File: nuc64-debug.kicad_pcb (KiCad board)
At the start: 2 copper layers, 17.1 x 22.9 mm, 10 parts, among them J1 SWD, J2 POW, SW1 BOOT, SW2 RST

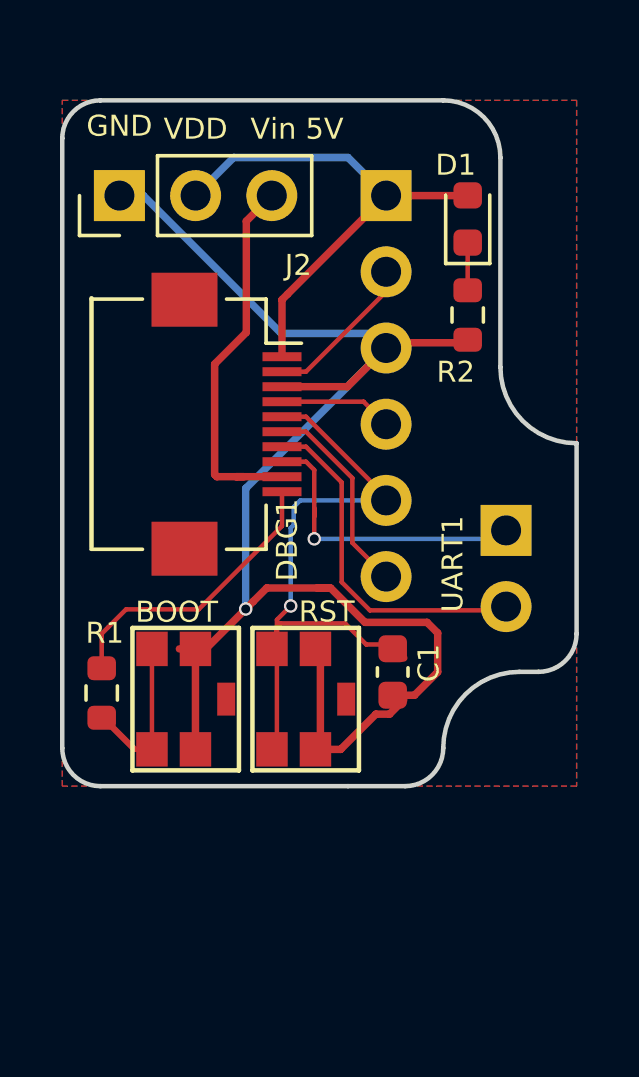
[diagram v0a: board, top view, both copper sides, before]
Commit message: [#32/#388] Boot0-button pulls high; updated symbols
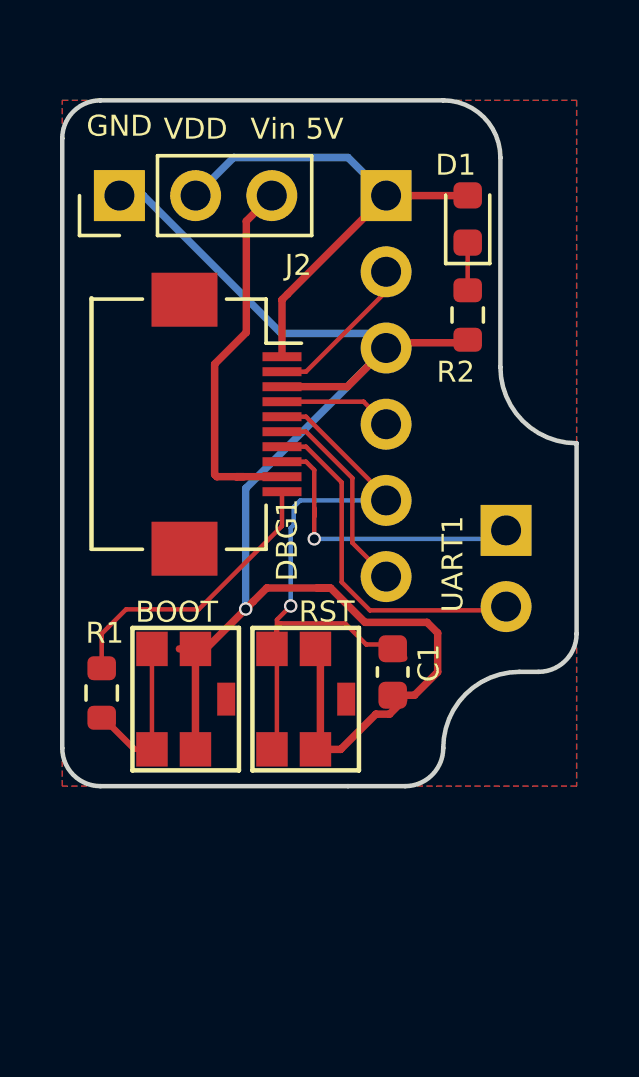
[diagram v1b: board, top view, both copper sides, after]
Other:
- net class Default removed
- net class power removed
- board text added: "CAMPO.SEESSLEN.NET NUC64DEBUG V0.3.x"
- board text removed: "CAMPO.SEESSLEN.NET NUC64DEBUG V0.2.x 20210714"

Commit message: Finished routing
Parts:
- added C2: 100n, Capacitor_SMD:C_0603_1608Metric, B.Cu at (112.0, 94.0)
- added R3: 330, Resistor_SMD:R_0603_1608Metric, B.Cu at (120.0, 94.0)
- C1, R1: moved to B.Cu
- D1: value LED -> LED Violet
- DBG1: footprint footprints:Hirose_FH12-10S-0.5SH_1x10_P0.5mm_Horizontal -> Connector_FFC-FPC:Hirose_FH12-10S-0.5SH_1x10-1MP_P0.50mm_Horizontal
- R2: value R -> 2K
- SW1, SW2: footprint footprints:panasonic_evpa302k -> Button_Switch_SMD:SW_SPST_Omron_B3FS-105xP
- moved SW2 6.48 mm to (120.7, 92.7)
- moved C1 5.02 mm to (120.0, 92.0), turned to 180 degrees
- moved SW1 4.80 mm to (112.3, 92.7)
- moved R1 4.79 mm to (112.0, 92.0), turned to 180 degrees
- moved J2 2.54 mm to (110.5, 68.6)
- moved DBG1 1.74 mm to (113.5, 78.8)
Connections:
- D1 pad 2: /VDD -> VDD
- DBG1 pad 1: /VDD -> VDD
- J1 pad 1: /VDD -> VDD
- J2 pad 2: /VDD -> VDD
- SW1 pad 2: GND -> VDD
- SW2 pad 1: /NRST -> Net-(R3-Pad2)
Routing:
- net VDD: track 0.00 -> 50.4 mm, vias 0 -> 1
- net GND: track 52.0 -> 99.0 mm, vias 1 -> 8
- net /VDD: track 17.0 -> 0.00 mm
- net Net-(R3-Pad2): track 0.00 -> 14.3 mm, vias 0 -> 1
- net Net-(R1-Pad2): track 7.05 -> 15.8 mm, vias 0 -> 1
- net Net-(DBG1-Pin_8): track 10.3 -> 17.3 mm, vias 1 -> 0
- net Net-(DBG1-Pin_10): track 9.79 -> 14.9 mm, vias 0 -> 1
- net /NRST: track 22.7 -> 18.5 mm, vias 1 -> 0
- net Net-(DBG1-Pin_7): track 11.7 -> 12.8 mm
- net Net-(DBG1-Pin_9): track 12.6 -> 13.3 mm
- net /SWDIO: track 3.78 -> 4.34 mm
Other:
- board size 17.1 x 22.9 mm -> 17.1 x 31.8 mm
- board text added: "20260117"

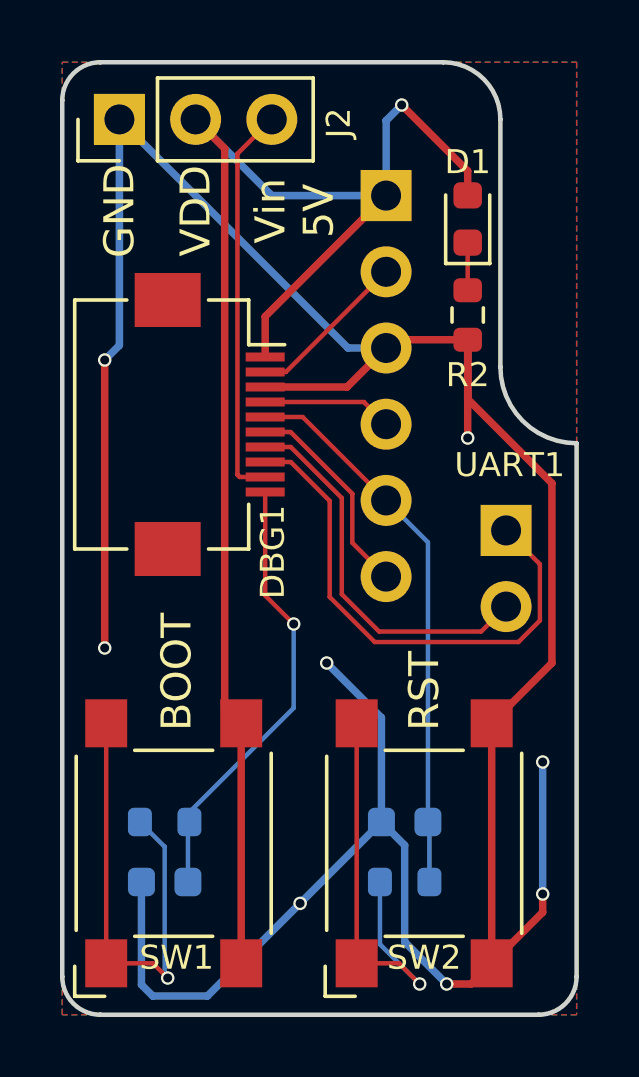
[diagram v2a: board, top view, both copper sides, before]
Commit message: Fixed trace width
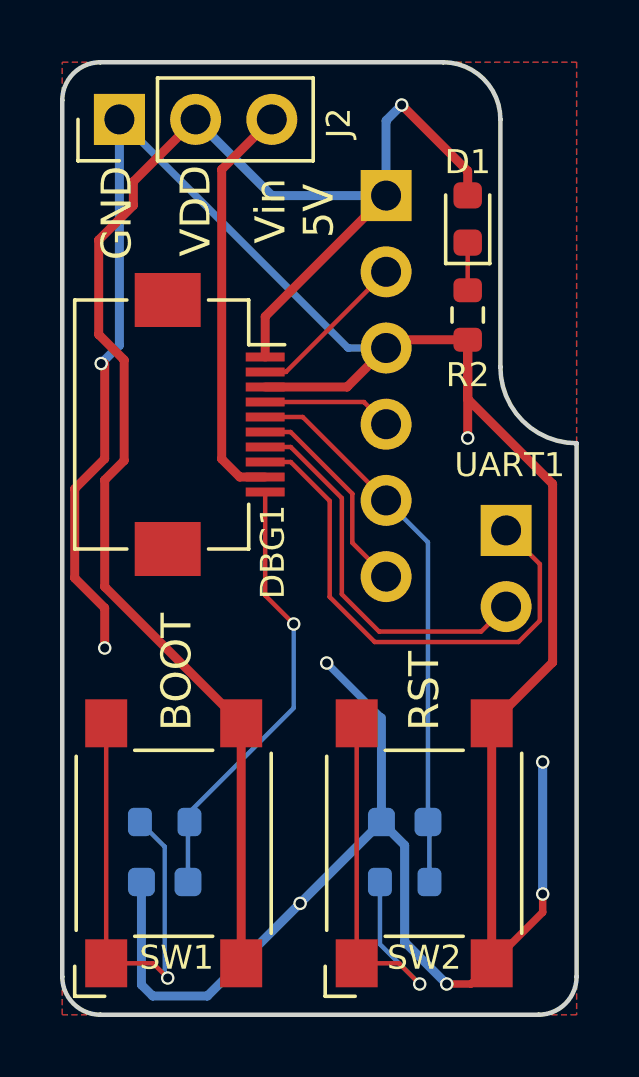
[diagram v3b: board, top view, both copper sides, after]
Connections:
- net Net-(DBG1-Pin_9) renamed VBUS
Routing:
- net VDD: track 50.4 -> 53.6 mm
- net GND: track 99.0 -> 100.0 mm
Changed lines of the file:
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@@
 	(net 8 "Net-(D1-K)")
 	(net 9 "VDD")
-	(net 10 "Net-(DBG1-Pin_9)")
+	(net 10 "VBUS")
 	(net 11 "Net-(DBG1-Pin_8)")
 	(net 12 "Net-(DBG1-Pin_7)")
@@
 			(layers "*.Cu" "*.Mask")
 			(remove_unused_layers no)
-			(net 10 "Net-(DBG1-Pin_9)")
+			(net 10 "VBUS")
 			(pinfunction "Pin_3")
 			(pintype "passive")
@@
 			(size 0.3 1.3)
 			(layers "F.Cu" "F.Mask" "F.Paste")
-			(net 10 "Net-(DBG1-Pin_9)")
+			(net 10 "VBUS")
 			(pinfunction "Pin_9")
 			(pintype "passive")
@@
 	)
 	(gr_text "GND"
-		(at 110.49 71.628 90)
+		(at 110.4 71.7 90)
 		(layer "F.SilkS")
 		(effects
@@
 		(start 122.1 75.925)
 		(end 119.655 75.925)
-		(width 0.25)
+		(width 0.3)
 		(layer "F.Cu")
 		(net 5)
 	)
 	(segment
-		(start 110 76.6)
-		(end 110 86.2)
-		(width 0.25)
+		(start 110 84.867106)
+		(end 109 83.867106)
+		(width 0.3)
 		(layer "F.Cu")
 		(net 5)
 	)
 	(segment
-		(start 122.1 77.9)
-		(end 122.1 75.925)
-		(width 0.25)
+		(start 109 83.867106)
+		(end 109 80.892893)
+		(width 0.3)
 		(layer "F.Cu")
 		(net 5)
@@
 		(start 122.1 75.925)
 		(end 122.1 79.2)
-		(width 0.25)
+		(width 0.3)
+		(layer "F.Cu")
+		(net 5)
+	)
+	(segment
+		(start 124.931 80.731)
+		(end 124.931 86.679)
+		(width 0.3)
+		(layer "F.Cu")
+		(net 5)
+	)
+	(segment
+		(start 124.931 86.679)
+		(end 122.9 88.71)
+		(width 0.3)
 		(layer "F.Cu")
 		(net 5)
@@
 		(start 115.35 77.5)
 		(end 118.08 77.5)
-		(width 0.25)
+		(width 0.3)
 		(layer "F.Cu")
 		(net 5)
 	)
 	(segment
-		(start 124.907 80.707)
-		(end 122.1 77.9)
-		(width 0.25)
+		(start 110 79.892894)
+		(end 110 76.734884)
+		(width 0.3)
 		(layer "F.Cu")
 		(net 5)
 	)
 	(segment
-		(start 124.907 86.703)
-		(end 124.907 80.707)
-		(width 0.25)
+		(start 109 80.892893)
+		(end 110 79.892894)
+		(width 0.3)
 		(layer "F.Cu")
 		(net 5)
 	)
 	(segment
-		(start 122.9 96.71)
-		(end 122.9 88.71)
-		(width 0.25)
+		(start 110 76.734884)
+		(end 109.982558 76.717442)
+		(width 0.3)
 		(layer "F.Cu")
 		(net 5)
 	)
 	(segment
-		(start 122.9 88.71)
-		(end 124.907 86.703)
-		(width 0.25)
+		(start 122.9 96.71)
+		(end 122.9 88.71)
+		(width 0.3)
 		(layer "F.Cu")
 		(net 5)
@@
 	)
 	(segment
+		(start 122.1 75.925)
+		(end 122.1 77.9)
+		(width 0.3)
+		(layer "F.Cu")
+		(net 5)
+	)
+	(segment
 		(start 118.08 77.5)
 		(end 119.38 76.2)
-		(width 0.25)
+		(width 0.3)
+		(layer "F.Cu")
+		(net 5)
+	)
+	(segment
+		(start 109.982558 76.717442)
+		(end 109.882558 76.717442)
+		(width 0.3)
 		(layer "F.Cu")
 		(net 5)
@@
 		(net 5)
 	)
+	(segment
+		(start 122.1 77.9)
+		(end 124.931 80.731)
+		(width 0.3)
+		(layer "F.Cu")
+		(net 5)
+	)
+	(segment
+		(start 110 86.2)
+		(end 110 84.867106)
+		(width 0.3)
+		(layer "F.Cu")
+		(net 5)
+	)
 	(via
 		(at 124.6 94.4)
@@
 	)
 	(via
-		(at 110 76.6)
+		(at 109.882558 76.717442)
 		(size 0.45)
 		(drill 0.3)
@@
 		(start 111.6 97.8)
 		(end 111.225 97.425)
-		(width 0.25)
+		(width 0.3)
 		(layer "B.Cu")
 		(net 5)
@@
 		(start 119.225 92)
 		(end 119.999 92.774)
-		(width 0.25)
+		(width 0.3)
 		(layer "B.Cu")
 		(net 5)
@@
 		(start 111.225 97.425)
 		(end 111.225 94)
-		(width 0.25)
+		(width 0.3)
 		(layer "B.Cu")
 		(net 5)
@@
 		(start 116.5125 94.7125)
 		(end 113.425 97.8)
-		(width 0.25)
+		(width 0.3)
 		(layer "B.Cu")
 		(net 5)
@@
 		(start 119.999 92.774)
 		(end 119.999 95.999)
-		(width 0.25)
+		(width 0.3)
 		(layer "B.Cu")
 		(net 5)
@@
 		(start 119.225 92)
 		(end 119.225 88.525)
-		(width 0.25)
+		(width 0.3)
 		(layer "B.Cu")
 		(net 5)
 	)
 	(segment
-		(start 124.6 94.4)
-		(end 124.6 90)
-		(width 0.25)
+		(start 110.49 76.11)
+		(end 109.882558 76.717442)
+		(width 0.3)
 		(layer "B.Cu")
 		(net 5)
 	)
 	(segment
-		(start 110.49 76.11)
-		(end 110 76.6)
-		(width 0.25)
+		(start 124.6 94.4)
+		(end 124.6 90)
+		(width 0.3)
 		(layer "B.Cu")
 		(net 5)
@@
 		(start 119.225 92)
 		(end 116.5125 94.7125)
-		(width 0.25)
+		(width 0.3)
 		(layer "B.Cu")
 		(net 5)
@@
 		(start 119.999 95.999)
 		(end 121.4 97.4)
-		(width 0.25)
+		(width 0.3)
 		(layer "B.Cu")
 		(net 5)
@@
 		(start 113.425 97.8)
 		(end 111.6 97.8)
-		(width 0.25)
+		(width 0.3)
 		(layer "B.Cu")
 		(net 5)
@@
 	)
 	(segment
-		(start 110.49 68.58)
-		(end 110.49 76.11)
+		(start 118.11 76.2)
+		(end 119.38 76.2)
 		(width 0.25)
 		(layer "B.Cu")
@@
 	)
 	(segment
-		(start 118.11 76.2)
-		(end 119.38 76.2)
-		(width 0.25)
+		(start 110.49 68.58)
+		(end 110.49 76.11)
+		(width 0.3)
 		(layer "B.Cu")
 		(net 5)
@@
 		(start 122.1 70.3)
 		(end 122.1 71.1125)
-		(width 0.25)
+		(width 0.3)
 		(layer "F.Cu")
 		(net 9)
 	)
 	(segment
-		(start 114.55 88.71)
-		(end 114 88.16)
-		(width 0.25)
+		(start 110.649 79.951)
+		(end 110 80.6)
+		(width 0.3)
 		(layer "F.Cu")
 		(net 9)
@@
 		(start 119.9 68.1)
 		(end 122.1 70.3)
-		(width 0.25)
+		(width 0.3)
+		(layer "F.Cu")
+		(net 9)
+	)
+	(segment
+		(start 113.03 68.58)
+		(end 110.955 70.655)
+		(width 0.3)
 		(layer "F.Cu")
 		(net 9)
@@
 		(start 114.55 96.71)
 		(end 114.55 88.71)
-		(width 0.25)
+		(width 0.3)
 		(layer "F.Cu")
 		(net 9)
 	)
 	(segment
-		(start 115.35 76.5)
-		(end 115.35 75.15)
-		(width 0.25)
+		(start 110 80.6)
+		(end 110 84.16)
+		(width 0.3)
 		(layer "F.Cu")
 		(net 9)
@@
 		(start 115.35 75.15)
 		(end 119.38 71.12)
-		(width 0.25)
+		(width 0.3)
 		(layer "F.Cu")
 		(net 9)
 	)
 	(segment
-		(start 114 88.16)
-		(end 114 69.55)
-		(width 0.25)
+		(start 110.649 76.6)
+		(end 110.649 79.951)
+		(width 0.3)
 		(layer "F.Cu")
 		(net 9)
 	)
 	(segment
-		(start 114 69.55)
-		(end 113.03 68.58)
-		(width 0.25)
+		(start 110.955 71.445)
+		(end 109.8 72.6)
+		(width 0.3)
+		(layer "F.Cu")
+		(net 9)
+	)
+	(segment
+		(start 115.35 76.5)
+		(end 115.35 75.15)
+		(width 0.3)
+		(layer "F.Cu")
+		(net 9)
+	)
+	(segment
+		(start 109.8 75.751)
+		(end 110.649 76.6)
+		(width 0.3)
+		(layer "F.Cu")
+		(net 9)
+	)
+	(segment
+		(start 110.955 70.655)
+		(end 110.955 71.445)
+		(width 0.3)
+		(layer "F.Cu")
+		(net 9)
+	)
+	(segment
+		(start 110 84.16)
+		(end 114.55 88.71)
+		(width 0.3)
+		(layer "F.Cu")
+		(net 9)
+	)
+	(segment
+		(start 109.8 72.6)
+		(end 109.8 75.751)
+		(width 0.3)
 		(layer "F.Cu")
 		(net 9)
@@
 		(start 119.38 71.12)
 		(end 119.38 68.62)
-		(width 0.25)
+		(width 0.3)
 		(layer "B.Cu")
 		(net 9)
@@
 		(start 119.38 71.12)
 		(end 115.57 71.12)
-		(width 0.25)
+		(width 0.3)
 		(layer "B.Cu")
 		(net 9)
@@
 		(start 119.38 68.62)
 		(end 119.9 68.1)
-		(width 0.25)
+		(width 0.3)
 		(layer "B.Cu")
 		(net 9)
@@
 		(start 115.57 71.12)
 		(end 113.03 68.58)
-		(width 0.25)
+		(width 0.3)
 		(layer "B.Cu")
 		(net 9)
 	)
 	(segment
-		(start 114.424 69.726)
+		(start 113.9 70.25)
 		(end 115.57 68.58)
-		(width 0.15)
+		(width 0.3)
 		(layer "F.Cu")
 		(net 10)
 	)
 	(segment
-		(start 114.424 80.426)
-		(end 114.424 69.726)
-		(width 0.15)
+		(start 113.9 79.9)
+		(end 113.9 70.25)
+		(width 0.3)
 		(layer "F.Cu")
 		(net 10)
@@
 	(segment
 		(start 115.35 80.5)
-		(end 114.498 80.5)
-		(width 0.15)
+		(end 114.5 80.5)
+		(width 0.3)
 		(layer "F.Cu")
 		(net 10)
 	)
 	(segment
-		(start 114.498 80.5)
-		(end 114.424 80.426)
-		(width 0.15)
+		(start 114.5 80.5)
+		(end 113.9 79.9)
+		(width 0.3)
 		(layer "F.Cu")
 		(net 10)

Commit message: Shrink
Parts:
- added C3: 10n, Capacitor_SMD:C_0603_1608Metric, B.Cu at (115.8, 81.3)
- added C4: 10µ, Capacitor_SMD:C_0603_1608Metric, B.Cu at (115.8, 84.5)
- added C5: 100n, Capacitor_SMD:C_0603_1608Metric, B.Cu at (115.8, 78.1)
- R2: moved to B.Cu
- moved R2 7.71 mm to (119.2, 67.9), turned to 180 degrees
- moved D1 4.89 mm to (119.2, 67.9), turned to 180 degrees
- moved SW2 1.42 mm to (120.0, 91.4)
- moved SW1 1.27 mm to (112.3, 91.4)
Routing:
- net GND: track 100.0 -> 112.0 mm, vias 8 -> 7
- net VDD: track 53.6 -> 59.8 mm
- net Net-(R3-Pad2): track 14.3 -> 12.7 mm
- net Net-(D1-K): track 1.59 -> 3.05 mm, vias 0 -> 1
- net Net-(R1-Pad2): track 15.8 -> 15.1 mm
- net Net-(DBG1-Pin_7): track 12.8 -> 12.2 mm
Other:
- board size 17.1 x 31.8 mm -> 17.1 x 30.5 mm

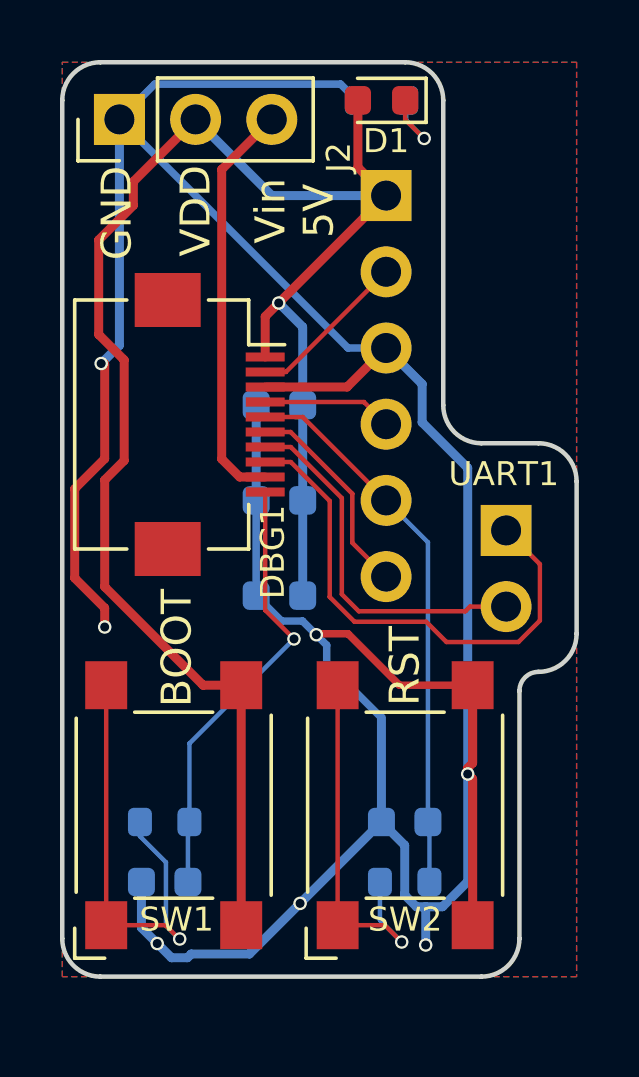
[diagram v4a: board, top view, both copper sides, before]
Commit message: Added UART LEDs
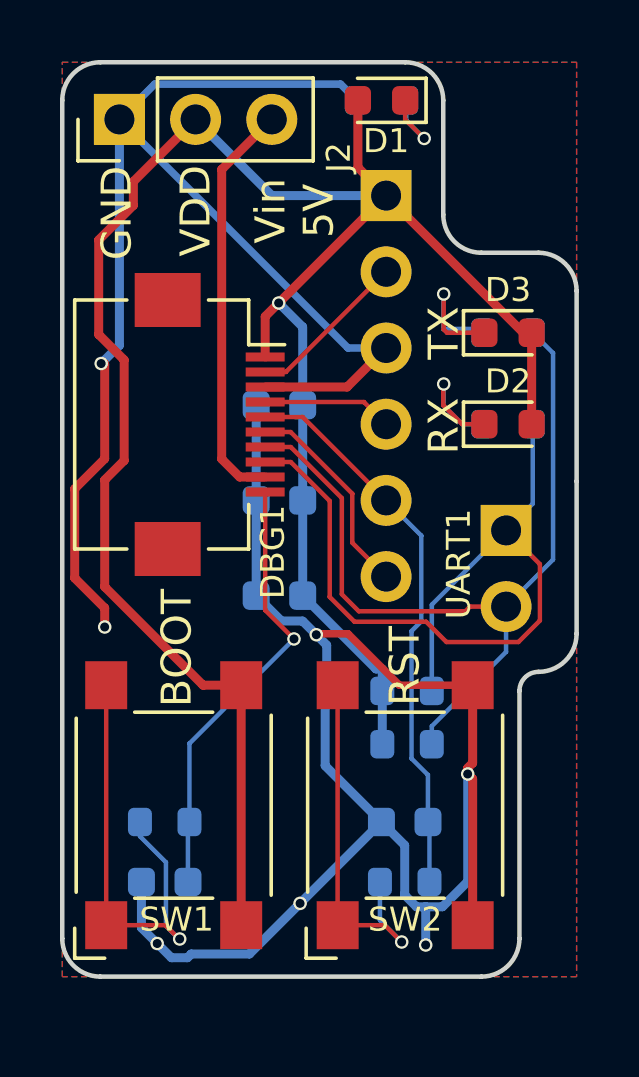
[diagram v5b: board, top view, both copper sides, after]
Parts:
- added D2: RX, LED_SMD:LED_0603_1608Metric, F.Cu at (123.4, 78.7)
- added D3: TX, LED_SMD:LED_0603_1608Metric, F.Cu at (123.4, 75.7)
- added R4: 1K, Resistor_SMD:R_0603_1608Metric, B.Cu at (120.1, 87.6)
- added R5: 1K, Resistor_SMD:R_0603_1608Metric, B.Cu at (120.1, 89.4)
- added R6: 680, Resistor_SMD:R_0603_1608Metric, B.Cu at (123.4, 78.7)
- added R7: 680, Resistor_SMD:R_0603_1608Metric, B.Cu at (123.4, 75.7)
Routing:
- net VDD: track 59.8 -> 75.7 mm
- net Net-(DBG1-Pin_7): track 12.2 -> 27.9 mm
- net GND: track 112.0 -> 96.5 mm
- net Net-(DBG1-Pin_8): track 17.3 -> 27.6 mm
- net Net-(D3-K): track 0.00 -> 5.14 mm, vias 0 -> 1
- net Net-(D2-K): track 0.00 -> 4.65 mm, vias 0 -> 1
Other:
- outline, holes or cut-outs redrawn

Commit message: Added mounting hole for soldering
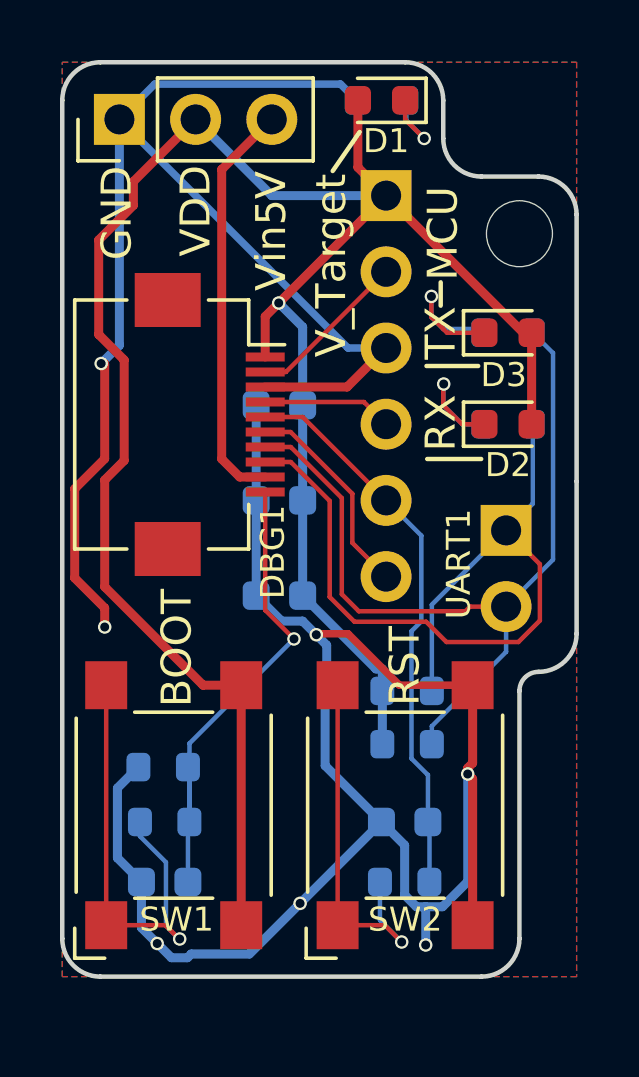
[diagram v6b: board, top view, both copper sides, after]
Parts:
- added H1: MountingHole, MountingHole:MountingHole_2.2mm_M2_DIN965, F.Cu at (123.8, 72.4)
- added R8: 1M, Resistor_SMD:R_0603_1608Metric, B.Cu at (112.0, 90.2)
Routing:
- net GND: track 96.5 -> 100.9 mm
- net Net-(DBG1-Pin_10): track 14.9 -> 16.7 mm
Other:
- outline, holes or cut-outs redrawn
- board text added: "MCU"
- board text added: "V_Target"
- board text added: "Vin5V"
- board text removed: "Vin 5V"

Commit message: Added Brezel
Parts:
- added G***: LOGO, Campo:brezel_silk, B.Cu at (112.4, 73.9)
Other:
- board text added: "NUC64DEBUG V0.3.x"
- board text added: "SEESSLEN.NET"
- board text removed: "CAMPO.SEESSLEN.NET NUC64DEBUG V0.3.x"
